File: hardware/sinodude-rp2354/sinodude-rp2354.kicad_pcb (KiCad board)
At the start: 2 copper layers, 75 x 40 mm, 93 parts, among them J1 USB-C, J2 SWD TC2030-IDC latching, J4 DUT, Q1 2N7002, SW1 BOOTSEL, SW2 RESET, U1 RP2354A, U2 AMS1117-3.3, U3 TPS2114APW, U4 SN74LVC8T245PW, U5 SN74LVC1T45DBV, U6 SN74LVC1T45DBV, Y1 12MHz/CL10pF/ESR50R/ABM8-272-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

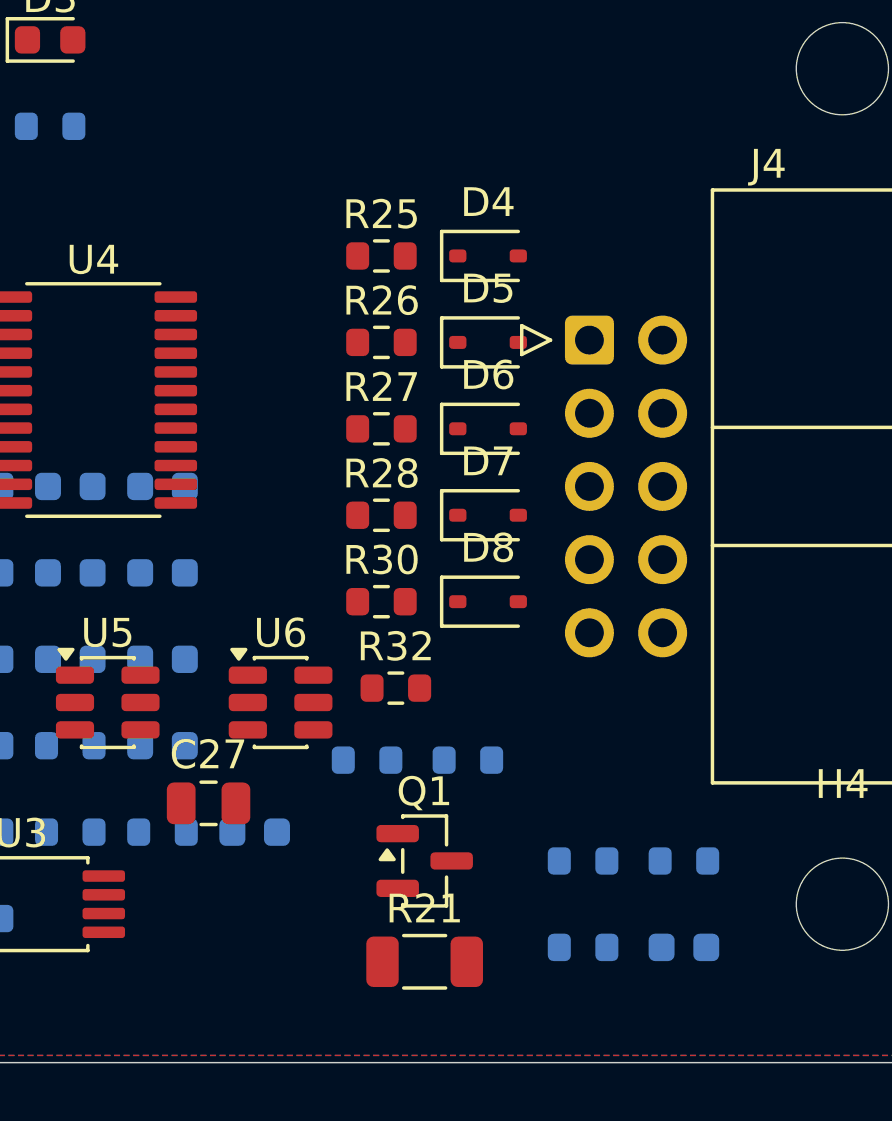
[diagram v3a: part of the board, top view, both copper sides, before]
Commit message: hardware: route the DUT-side bundle, fix reversed series resistors
Route the six DUT signals: U4/U5/U6 B-side, through the 22R series column,
tapping the ESD diodes, and into J4 between its pin rows. Strict 45 degrees,
parallel bundle, in the Glasgow idiom.

Placement fixes the net map exposed:
- R25/R26/R27/R30 were reversed, their U4-side pad facing away from U4, so
  every one of those traces would have doubled back on itself.
- The ESD diodes sat on the signal path, blocking it. They now sit in the
  gaps between signal lines and tap upward with a short stub.
- R32 overlapped U6's courtyard.
- Shifted both columns left 1 mm so the NRST diagonal clears D7's pad; it
  missed by 0.16 mm before.

NRST's final leg drops to the bottom through one via to pass under DATA, the
one crossing the pin ordering makes unavoidable.

DRC after refilling zones: no shorts, no crossings, no clearance or courtyard
violations. Remaining are 138 unconnected (the unrouted rest of the board),
9 drill_out_of_range from the QFN thermal vias at 0.2 mm against a 0.3 mm
minimum, and J1's stock footprint holding 0.194 mm between its own GND pads
and its own mounting holes.
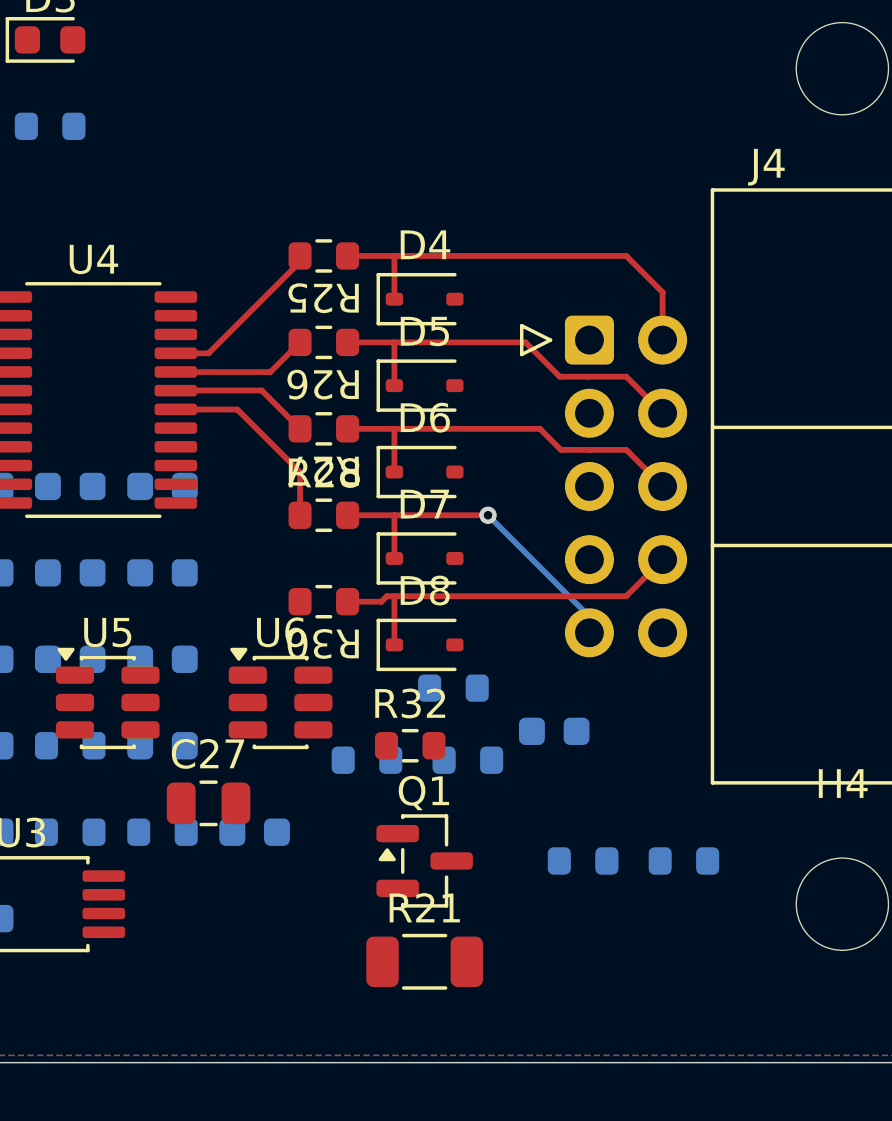
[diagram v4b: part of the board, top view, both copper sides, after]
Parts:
- moved R33 10.1 mm to (157.0, 127.0)
- moved C36 8.75 mm to (160.5, 128.5)
- moved D4 2.66 mm to (156.0, 113.5)
- moved D5 2.66 mm to (156.0, 116.5)
- moved D6 2.66 mm to (156.0, 119.5)
- moved D7 2.66 mm to (156.0, 122.5)
- moved D8 2.66 mm to (156.0, 125.5)
- moved R32 2.06 mm to (155.5, 129.0)
- moved R25 2.00 mm to (152.5, 112.0), turned to 180 degrees
- moved R26 2.00 mm to (152.5, 115.0), turned to 180 degrees
- moved R27 2.00 mm to (152.5, 118.0), turned to 180 degrees
- moved R28 2.00 mm to (152.5, 121.0)
- moved R30 2.00 mm to (152.5, 124.0), turned to 180 degrees
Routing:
- net Net-(D4-A1): track 0.00 -> 14.6 mm
- net Net-(D5-A1): track 0.00 -> 13.5 mm
- net Net-(D6-A1): track 0.00 -> 13.3 mm
- net Net-(D8-A1): track 0.00 -> 13.2 mm
- net Net-(D7-A1): track 0.00 -> 11.9 mm, vias 0 -> 1
- net NRST_B: track 0.00 -> 6.71 mm
- net TCK_B: track 0.00 -> 5.92 mm
- net TMS_B: track 0.00 -> 4.87 mm
- net TDI_B: track 0.00 -> 4.74 mm

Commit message: hardware: route crystal, LEDs and LED anode vias
XIN, Net-(C23-Pad1), LED_ACT, LED_ERR and both LED anode via drops are routed.
LED_ERR now runs along y=103 above the LEDs rather than y=107, where it would
have crossed LED_ACT's vertical.

XOUT is left unrouted deliberately. The crystal's XIN terminal is on its left
but U1's XIN pin (21) sits to the right of XOUT (22), so the two nets have to
swap sides, and U1's top row at 0.4 mm pitch leaves nowhere to put the via
that would carry one under the other. The fix is to rotate Y1 180 degrees and
mirror C22/C23/R6 to the other side of the crystal, which also needs C6 and
LED_ERR moved out of the way. Left as a deliberate gap rather than shipped as
a short.

DRC: no shorts, no crossings, no clearance or courtyard violations.
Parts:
- moved C14 2.00 mm to (127.8, 113.8)
- moved C6 2.00 mm to (124.6, 113.8)
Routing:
- net LED_ERR: track 0.00 -> 38.8 mm
- net LED_ACT: track 0.00 -> 18.7 mm
- net XIN: track 0.00 -> 8.94 mm
- net Net-(C23-Pad1): track 0.00 -> 6.28 mm
- net Net-(D3-A): track 0.00 -> 3.00 mm, vias 0 -> 1
- net Net-(D2-A): track 0.00 -> 3.00 mm, vias 0 -> 1
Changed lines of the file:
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@@
 	(footprint "Capacitor_SMD:C_0603_1608Metric"
 		(layer "F.Cu")
-		(at 129.8 113.8)
+		(at 127.8 113.8)
 		(property "Reference" "C14"
 			(at 0 -1.43 0)
@@
 	(footprint "Capacitor_SMD:C_0603_1608Metric"
 		(layer "F.Cu")
-		(at 126.6 113.8)
+		(at 124.6 113.8)
 		(property "Reference" "C6"
 			(at 0 -1.429999 0)
@@
 	)
 	(segment
+		(start 131.6 115.5)
+		(end 131.6 116.55)
+		(width 0.2)
+		(layer "F.Cu")
+		(net "LED_ACT")
+	)
+	(segment
+		(start 138.21 115.5)
+		(end 131.6 115.5)
+		(width 0.2)
+		(layer "F.Cu")
+		(net "LED_ACT")
+	)
+	(segment
+		(start 138.21 104.5)
+		(end 138.21 115.5)
+		(width 0.2)
+		(layer "F.Cu")
+		(net "LED_ACT")
+	)
+	(segment
+		(start 129.5 111.35)
+		(end 129.5 114.45)
+		(width 0.2)
+		(layer "F.Cu")
+		(net "XIN")
+	)
+	(segment
+		(start 129.5 114.45)
+		(end 130.8 115.75)
+		(width 0.2)
+		(layer "F.Cu")
+		(net "XIN")
+	)
+	(segment
+		(start 129.5 111.35)
+		(end 126.3 111.35)
+		(width 0.2)
+		(layer "F.Cu")
+		(net "XIN")
+	)
+	(segment
+		(start 130.8 115.75)
+		(end 130.8 116.55)
+		(width 0.2)
+		(layer "F.Cu")
+		(net "XIN")
+	)
+	(segment
+		(start 142.21 104.5)
+		(end 142.21 103)
+		(width 0.2)
+		(layer "F.Cu")
+		(net "LED_ERR")
+	)
+	(segment
+		(start 123 115.5)
+		(end 128.4 115.5)
+		(width 0.2)
+		(layer "F.Cu")
+		(net "LED_ERR")
+	)
+	(segment
+		(start 128.4 115.5)
+		(end 128.4 116.55)
+		(width 0.2)
+		(layer "F.Cu")
+		(net "LED_ERR")
+	)
+	(segment
+		(start 124.5 103)
+		(end 123 104.5)
+		(width 0.2)
+		(layer "F.Cu")
+		(net "LED_ERR")
+	)
+	(segment
+		(start 142.21 103)
+		(end 124.5 103)
+		(width 0.2)
+		(layer "F.Cu")
+		(net "LED_ERR")
+	)
+	(segment
+		(start 123 104.5)
+		(end 123 115.5)
+		(width 0.2)
+		(layer "F.Cu")
+		(net "LED_ERR")
+	)
+	(segment
 		(start 153.32 112)
 		(end 163 112)
@@
 	)
 	(segment
+		(start 134.5 111.28)
+		(end 134.5 113.12)
+		(width 0.2)
+		(layer "F.Cu")
+		(net "Net-(C23-Pad1)")
+	)
+	(segment
+		(start 131.699999 109.65)
+		(end 132.87 109.65)
+		(width 0.2)
+		(layer "F.Cu")
+		(net "Net-(C23-Pad1)")
+	)
+	(segment
+		(start 134.5 113.12)
+		(end 133.82 113.8)
+		(width 0.2)
+		(layer "F.Cu")
+		(net "Net-(C23-Pad1)")
+	)
+	(segment
+		(start 132.87 109.65)
+		(end 134.5 111.28)
+		(width 0.2)
+		(layer "F.Cu")
+		(net "Net-(C23-Pad1)")
+	)
+	(segment
+		(start 139.79 104.5)
+		(end 139.8 106.1)
+		(width 0.2)
+		(layer "F.Cu")
+		(net "Net-(D2-A)")
+	)
+	(via
+		(at 139.8 106.1)
+		(size 0.6)
+		(drill 0.3)
+		(layers "F.Cu" "B.Cu")
+		(net "Net-(D2-A)")
+	)
+	(segment
+		(start 139.8 106.1)
+		(end 139.82 107.5)
+		(width 0.2)
+		(layer "B.Cu")
+		(net "Net-(D2-A)")
+	)
+	(segment
 		(start 150.345 116.67)
 		(end 151.675 118)
@@
 		(net "Net-(D6-A1)")
 	)
+	(segment
+		(start 143.79 104.5)
+		(end 143.8 106.1)
+		(width 0.2)
+		(layer "F.Cu")
+		(net "Net-(D3-A)")
+	)
+	(via
+		(at 143.8 106.1)
+		(size 0.6)
+		(drill 0.3)
+		(layers "F.Cu" "B.Cu")
+		(net "Net-(D3-A)")
+	)
+	(segment
+		(start 143.8 106.1)
+		(end 143.82 107.5)
+		(width 0.2)
+		(layer "B.Cu")
+		(net "Net-(D3-A)")
+	)
 	(zone

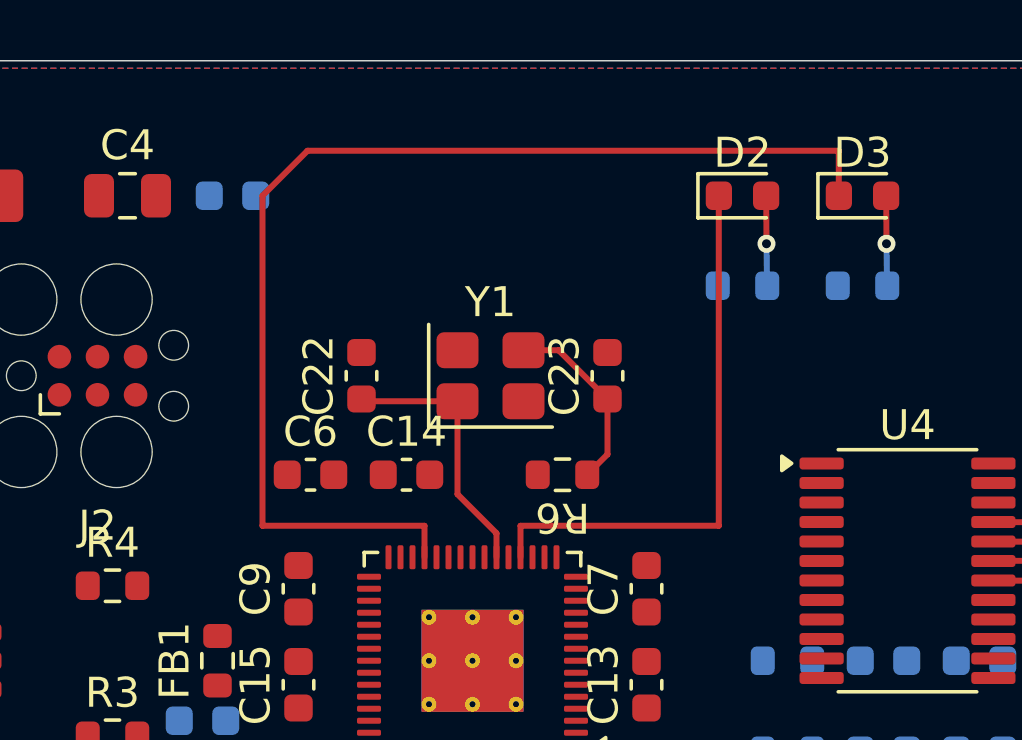
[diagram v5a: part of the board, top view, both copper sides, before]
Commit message: hardware: rework crystal block, route XIN/XOUT/C23 and both LEDs
Rotating Y1 180 degrees puts its XIN terminal upper-right and the C23-side
terminal lower-left, matching U1's pin order (XIN at 21 sits right of XOUT at
22). That removes the crossing that forced XOUT to be left unrouted, with no
via needed: XIN now comes down the right of the pair and XOUT the left.

Moved C6, C14, R6 and the crystal out of y=111..116 to leave a clear band
above U1 for the top-row fan-out. Ten signals have to escape that row and
there was no room for any of them before.

Deleted four orphaned segments from the crystal's old position. They had been
silently reassigned to GND when the parts moved, and one of them crossed XIN.

DRC: no shorts, no crossings, no clearance or courtyard violations.
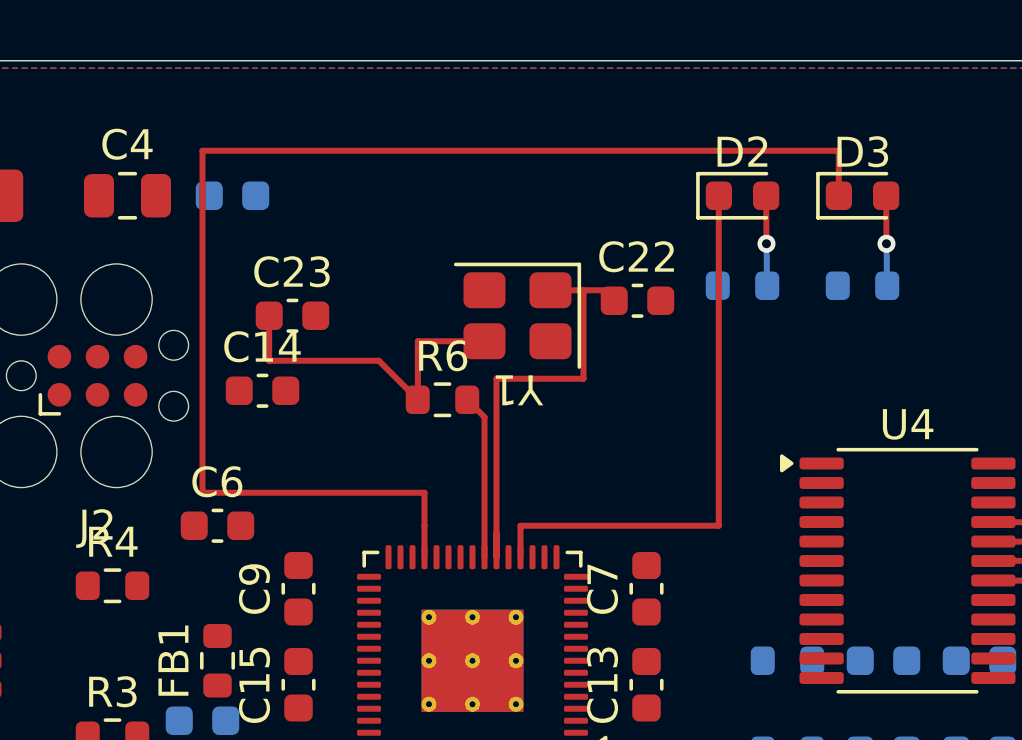
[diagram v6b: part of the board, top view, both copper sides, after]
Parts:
- moved C23 10.7 mm to (124.0, 108.5), turned to 0 degrees
- moved C22 9.53 mm to (135.5, 108.0), turned to 0 degrees
- moved C14 5.56 mm to (123.0, 111.0)
- moved R6 4.72 mm to (129.0, 111.3), turned to 0 degrees
- moved C6 3.54 mm to (121.5, 115.5)
- moved Y1 2.19 mm to (131.5, 108.5), turned to 180 degrees
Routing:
- net XIN: track 8.94 -> 14.7 mm
- net XOUT: track 0.00 -> 5.49 mm
- net Net-(C23-Pad1): track 6.28 -> 11.2 mm
- net LED_ERR: track 38.8 -> 43.7 mm
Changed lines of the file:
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@@
 	(footprint "Capacitor_SMD:C_0603_1608Metric"
 		(layer "F.Cu")
-		(at 127.8 113.8)
+		(at 123 111)
 		(property "Reference" "C14"
 			(at 0 -1.43 0)
@@
 	(footprint "Capacitor_SMD:C_0603_1608Metric"
 		(layer "F.Cu")
-		(at 124.6 113.8)
+		(at 121.5 115.5)
 		(property "Reference" "C6"
 			(at 0 -1.429999 0)
@@
 	(footprint "Crystal:Crystal_SMD_3225-4Pin_3.2x2.5mm"
 		(layer "F.Cu")
-		(at 130.6 110.5)
+		(at 131.5 108.5 180)
 		(property "Reference" "Y1"
-			(at 0 -2.45 0)
+			(at 0 -2.45 180)
 			(unlocked yes)
 			(layer "F.SilkS")
@@
 		)
 		(property "Value" "12MHz/CL10pF/ESR50R/ABM8-272-T3"
-			(at 0 2.45 0)
+			(at 0 2.45 180)
 			(unlocked yes)
 			(layer "F.SilkS")
@@
 		)
 		(property "Datasheet" ""
-			(at 0 0 0)
+			(at 0 0 180)
 			(layer "F.Fab")
 			(hide yes)
@@
 		)
 		(property "Description" ""
-			(at 0 0 0)
+			(at 0 0 180)
 			(layer "F.Fab")
 			(hide yes)
@@
 		(duplicate_pad_numbers_are_jumpers no)
 		(fp_line
-			(start -2.060001 -1.71)
-			(end -2.060001 1.71)
+			(start -2.060001 1.71)
+			(end 2.06 1.71)
 			(stroke
 				(width 0.12)
@@
 		)
 		(fp_line
-			(start -2.060001 1.71)
-			(end 2.06 1.71)
+			(start -2.060001 -1.71)
+			(end -2.060001 1.71)
 			(stroke
 				(width 0.12)
@@
 		)
 		(fp_text user "${REFERENCE}"
-			(at 0 0 0)
+			(at 0 0 180)
 			(unlocked yes)
 			(layer "F.Fab")
@@
 		)
 		(pad "1" smd roundrect
-			(at -1.1 0.85)
+			(at -1.1 0.85 180)
 			(size 1.4 1.2)
 			(layers "F.Cu" "F.Mask" "F.Paste")
@@
 		)
 		(pad "2" smd roundrect
-			(at 1.099999 0.85)
+			(at 1.099999 0.85 180)
 			(size 1.4 1.2)
 			(layers "F.Cu" "F.Mask" "F.Paste")
@@
 		)
 		(pad "3" smd roundrect
-			(at 1.099999 -0.85)
+			(at 1.099999 -0.85 180)
 			(size 1.4 1.2)
 			(layers "F.Cu" "F.Mask" "F.Paste")
@@
 		)
 		(pad "4" smd roundrect
-			(at -1.1 -0.85)
+			(at -1.1 -0.85 180)
 			(size 1.4 1.2)
 			(layers "F.Cu" "F.Mask" "F.Paste")
@@
 	(footprint "Capacitor_SMD:C_0603_1608Metric"
 		(layer "F.Cu")
-		(at 126.3 110.5 90)
+		(at 135.5 108)
 		(property "Reference" "C22"
-			(at 0 -1.43 90)
+			(at 0 -1.43 0)
 			(unlocked yes)
 			(layer "F.SilkS")
@@
 		)
 		(property "Value" "15pF/50V/5%/C0G/C0603"
-			(at 0 1.43 90)
+			(at 0 1.43 0)
 			(unlocked yes)
 			(layer "F.SilkS")
@@
 		)
 		(property "Datasheet" ""
-			(at 0 0 90)
+			(at 0 0 0)
 			(layer "F.Fab")
 			(hide yes)
@@
 		)
 		(property "Description" ""
-			(at 0 0 90)
+			(at 0 0 0)
 			(layer "F.Fab")
 			(hide yes)
@@
 		)
 		(fp_text user "${REFERENCE}"
-			(at 0 0 90)
+			(at 0 0 0)
 			(unlocked yes)
 			(layer "F.Fab")
@@
 		)
 		(pad "1" smd roundrect
-			(at -0.775 0 90)
+			(at -0.775 0)
 			(size 0.9 0.95)
 			(layers "F.Cu" "F.Mask" "F.Paste")
@@
 		)
 		(pad "2" smd roundrect
-			(at 0.775 0 90)
+			(at 0.775 0)
 			(size 0.9 0.95)
 			(layers "F.Cu" "F.Mask" "F.Paste")
@@
 	(footprint "Resistor_SMD:R_0603_1608Metric"
 		(layer "F.Cu")
-		(at 133 113.8 180)
+		(at 129 111.3)
 		(property "Reference" "R6"
-			(at 0 -1.43 180)
+			(at 0 -1.43 0)
 			(unlocked yes)
 			(layer "F.SilkS")
@@
 		)
 		(property "Value" "1k"
-			(at 0 1.43 180)
+			(at 0 1.43 0)
 			(unlocked yes)
 			(layer "F.SilkS")
@@
 		)
 		(property "Datasheet" ""
-			(at 0 0 180)
+			(at 0 0 0)
 			(layer "F.Fab")
 			(hide yes)
@@
 		)
 		(property "Description" ""
-			(at 0 0 180)
+			(at 0 0 0)
 			(layer "F.Fab")
 			(hide yes)
@@
 		(duplicate_pad_numbers_are_jumpers no)
 		(fp_line
-			(start -0.237258 0.5225)
-			(end 0.237258 0.5225)
+			(start -0.237258 -0.5225)
+			(end 0.237258 -0.5225)
 			(stroke
 				(width 0.12)
@@
 		)
 		(fp_line
-			(start -0.237258 -0.5225)
-			(end 0.237258 -0.5225)
+			(start -0.237258 0.5225)
+			(end 0.237258 0.5225)
 			(stroke
 				(width 0.12)
@@
 		)
 		(fp_text user "${REFERENCE}"
-			(at 0 0 180)
+			(at 0 0 0)
 			(unlocked yes)
 			(layer "F.Fab")
@@
 		)
 		(pad "1" smd roundrect
-			(at -0.825 0 180)
+			(at -0.825 0)
 			(size 0.8 0.95)
 			(layers "F.Cu" "F.Mask" "F.Paste")
@@
 		)
 		(pad "2" smd roundrect
-			(at 0.825 0 180)
+			(at 0.825 0)
 			(size 0.8 0.95)
 			(layers "F.Cu" "F.Mask" "F.Paste")
@@
 	(footprint "Capacitor_SMD:C_0603_1608Metric"
 		(layer "F.Cu")
-		(at 134.5 110.5 90)
+		(at 124 108.5)
 		(property "Reference" "C23"
-			(at 0 -1.43 90)
+			(at 0 -1.43 0)
 			(unlocked yes)
 			(layer "F.SilkS")
@@
 		)
 		(property "Value" "15pF/50V/5%/C0G/C0603"
-			(at 0 1.43 90)
+			(at 0 1.43 0)
 			(unlocked yes)
 			(layer "F.SilkS")
@@
 		)
 		(property "Datasheet" ""
-			(at 0 0 90)
+			(at 0 0 0)
 			(layer "F.Fab")
 			(hide yes)
@@
 		)
 		(property "Description" ""
-			(at 0 0 90)
+			(at 0 0 0)
 			(layer "F.Fab")
 			(hide yes)
@@
 		)
 		(fp_text user "${REFERENCE}"
-			(at 0 0 90)
+			(at 0 0 0)
 			(unlocked yes)
 			(layer "F.Fab")
@@
 		)
 		(pad "1" smd roundrect
-			(at -0.775 0 90)
+			(at -0.775 0)
 			(size 0.9 0.95)
 			(layers "F.Cu" "F.Mask" "F.Paste")
@@
 		)
 		(pad "2" smd roundrect
-			(at 0.775 0 90)
+			(at 0.775 0)
 			(size 0.9 0.95)
 			(layers "F.Cu" "F.Mask" "F.Paste")
@@
 	)
 	(segment
-		(start 129.5 111.35)
-		(end 129.5 114.45)
+		(start 130.8 110.6)
+		(end 130.8 116.55)
+		(width 0.2)
+		(layer "F.Cu")
+		(net "XIN")
+	)
+	(segment
+		(start 133.699999 110.6)
+		(end 130.8 110.6)
 		(width 0.2)
 		(layer "F.Cu")
@@
 	)
 	(segment
-		(start 129.5 114.45)
-		(end 130.8 115.75)
+		(start 132.6 107.65)
+		(end 134.72 107.65)
 		(width 0.2)
 		(layer "F.Cu")
@@
 	)
 	(segment
-		(start 129.5 111.35)
-		(end 126.3 111.35)
+		(start 133.699999 107.65)
+		(end 133.699999 110.6)
 		(width 0.2)
 		(layer "F.Cu")
@@
 	)
 	(segment
+		(start 129.82 111.3)
+		(end 130.4 111.88)
+		(width 0.2)
+		(layer "F.Cu")
+		(net "XOUT")
+	)
+	(segment
+		(start 130.4 111.88)
+		(end 130.4 116.55)
+		(width 0.2)
+		(layer "F.Cu")
+		(net "XOUT")
+	)
+	(segment
 		(start 142.21 104.5)
 		(end 142.21 103)
@@
 	)
 	(segment
-		(start 123 115.5)
-		(end 128.4 115.5)
+		(start 142.21 103)
+		(end 121 103)
 		(width 0.2)
 		(layer "F.Cu")
@@
 	)
 	(segment
-		(start 128.4 115.5)
-		(end 128.4 116.55)
+		(start 128.4 114.4)
+		(end 128.4 115.5)
 		(width 0.2)
 		(layer "F.Cu")
@@
 	)
 	(segment
-		(start 124.5 103)
-		(end 123 104.5)
+		(start 128.4 115.5)
+		(end 128.4 116.55)
 		(width 0.2)
 		(layer "F.Cu")
@@
 	)
 	(segment
-		(start 142.21 103)
-		(end 124.5 103)
+		(start 121 103)
+		(end 121 114.4)
 		(width 0.2)
 		(layer "F.Cu")
@@
 	)
 	(segment
-		(start 123 104.5)
-		(end 123 115.5)
+		(start 121 114.4)
+		(end 128.4 114.4)
 		(width 0.2)
 		(layer "F.Cu")
@@
 	)
 	(segment
-		(start 134.5 111.28)
-		(end 134.5 113.12)
+		(start 130.4 109.35)
+		(end 128.18 109.35)
+		(width 0.2)
+		(layer "F.Cu")
+		(net "Net-(C23-Pad1)")
+	)
+	(segment
+		(start 123.22 110)
+		(end 126.88 110)
 		(width 0.2)
 		(layer "F.Cu")
@@
 	)
 	(segment
-		(start 131.699999 109.65)
-		(end 132.87 109.65)
+		(start 126.88 110)
+		(end 128.18 111.3)
 		(width 0.2)
 		(layer "F.Cu")
@@
 	)
 	(segment
-		(start 134.5 113.12)
-		(end 133.82 113.8)
+		(start 128.18 109.35)
+		(end 128.18 111.3)
 		(width 0.2)
 		(layer "F.Cu")
@@
 	)
 	(segment
-		(start 132.87 109.65)
-		(end 134.5 111.28)
+		(start 123.22 108.5)
+		(end 123.22 110)
 		(width 0.2)
 		(layer "F.Cu")
